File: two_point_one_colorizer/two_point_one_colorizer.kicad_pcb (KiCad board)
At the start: 2 copper layers, 100 x 100 mm, 83 parts, among them J1 rca, J2 rca, J3 Mini-DIN-4, J4 Barrel_Jack, J5 Conn_01x03, Q1 2N3904, SW1 SW_SPDT, SW2 SW_SPDT, U1 74HC14, U2 4053, U3 LM317, U4 LM1881, U5 74HC86, U6 4013, U7 LM393, U8 74LS221, U9 74LS221, Y1 Crystal

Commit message: revised all boards
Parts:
- added J6: Conn_01x03, Connector_PinHeader_2.54mm:PinHeader_1x03_P2.54mm_Vertical, F.Cu at (107.6, 92.2)
- added J7: Conn_02x08_Odd_Even, Connector_PinHeader_2.54mm:PinHeader_2x08_P2.54mm_Vertical, F.Cu at (182.9, 37.3)
- added R35: 1.5k, Resistor_THT:R_Axial_DIN0207_L6.3mm_D2.5mm_P7.62mm_Horizontal, F.Cu at (144.0, 47.9)
- added Y2: Crystal, Crystal:Crystal_HC49-4H_Vertical, F.Cu at (114.8, 92.5)
- J1, J2: footprint lib_fp:RCJ-024 -> lib_fp:tht_vertical_rca
- J3: value Mini-DIN-4 -> mini-din4; footprint lib_fp:MiniDin4-MD-40S -> lib_fp:mini-din-4-vertical_KMDVLX-4S-N-1
- R10: value 10k -> 1k
- R14: value 12k -> 1.5k
- R2: value 5k -> 5.1k
- R23, R29: value R -> 10k
- R26, R32: value 8.2k -> (lower than) 8.2k
- R7: value 1M -> 1m
- R9: value 1k -> 10k
- RV1, RV2, RV3, RV4, RV5, RV6: value 10k -> 10k_pot
- SW1, SW2: value SW_SPDT -> SPDT
- U2: value 4053 -> CD4053
- U6: value 4013 -> CD4013
- moved Y1 7.76 mm to (114.8, 86.4)
- moved J3 7.00 mm to (121.6, 43.8)
- moved C1 6.89 mm to (111.7, 81.9)
- moved C2 6.89 mm to (115.2, 81.9)
- moved C12 0.70 mm to (146.5, 62.2)
- moved R10 0.70 mm to (151.5, 54.7)
- moved R11 0.70 mm to (144.0, 58.2)
- moved R9 0.70 mm to (144.0, 51.2)
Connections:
- R10 pad 1: GND -> /sync_and_burst/black_and_sync
- U2 pad 3: GND -> /sync_and_burst/black_and_sync
- U6 pad 3: Net-(U4-Pad3) -> Net-(R10-Pad2)
- Y1 pad 1: Net-(C1-Pad1) -> Net-(J6-Pad3)
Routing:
- net Net-(R10-Pad2): track 15.1 -> 86.4 mm
- net Net-(U4-Pad3): track 68.4 -> 0.40 mm, vias 3 -> 0
- net /sync_and_burst/black_and_sync: track 0.00 -> 39.7 mm
- net Net-(C1-Pad1): track 21.3 -> 35.4 mm
- net +5V: track 560.3 -> 573.8 mm
- net Net-(J6-Pad3): track 0.00 -> 7.50 mm
- net Net-(J6-Pad1): track 0.00 -> 7.32 mm
- net Net-(C3-Pad2): track 24.4 -> 30.6 mm
- net GND: track 14.8 -> 20.4 mm
- net Net-(C2-Pad1): track 15.8 -> 18.7 mm
- net /sync_and_burst/burst_pulse: track 83.8 -> 84.5 mm
- net Net-(C15-Pad1): vias 1 -> 0
- net /colours/crystal: vias 1 -> 0
- net /colours/colour2: vias 2 -> 0
- net /colours/colour1: vias 3 -> 0
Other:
- board text added: "_^ XX"
- board text added: "two_point_one_colorizer v0_2 based on rob schafer design updated by cyberboy666"
- board text added: "underscores.shop"
- board text removed: "two_point_one_colorizer v0.1 by rob schafer pcb by cyberboy666"

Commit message: working on nexr version for colorizer and inverter
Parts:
- removed J5, J6: Conn_01x03, Connector_PinHeader_2.54mm:PinHeader_1x03_P2.54mm_Vertical
- removed REF** (x4): MountingHole_3.2mm_M3, MountingHole:MountingHole_3.2mm_M3
- added C21: 0.1n, Capacitor_THT:C_Disc_D4.7mm_W2.5mm_P5.00mm, F.Cu at (249.4, 78.2)
- added R36: 10k, Resistor_THT:R_Axial_DIN0207_L6.3mm_D2.5mm_P7.62mm_Horizontal, F.Cu at (211.4, 100.1)
- added RV7: 5k_trim, lib_fp:Pot_trim_3362_tayda, F.Cu at (213.6, 112.8)
- added RV8: 5k_trim, lib_fp:Pot_trim_3362_tayda, F.Cu at (221.5, 112.8)
- added RV9: 20k_pot, lib_fp:Potentiometer_Vertical_Large, F.Cu at (234.7, 86.2)
- added SW3: SPDT_slide, lib_fp:spdt_slide_switch_small_tayda, F.Cu at (279.9, 79.7)
- added SW4: SPDT_slide, lib_fp:spdt_slide_switch_small_tayda, F.Cu at (228.9, 99.1)
- added U11: 74HC4538, Package_DIP:DIP-16_W7.62mm_LongPads, F.Cu at (211.8, 78.3)
- R26, R32: value (lower than) 8.2k -> 1.5k
- R35: value 1.5k -> 1k (or 1.2k maybe)
- U1: value 74HC14 -> 4069
- U4: footprint Package_DIP:DIP-8_W7.62mm_LongPads -> lib_fp:DIP-SOIC-8
- moved U1 157.1 mm to (262.8, 78.3)
- moved U6 30.2 mm to (223.4, 78.3)
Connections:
- J3 pad 3: Net-(C3-Pad2) -> Net-(J3-Pad3)
- J3 pad 4: Net-(J3-Pad4) -> Net-(C3-Pad2)
- R26 pad 1: +5V -> Net-(R26-Pad1)
- R32 pad 1: +5V -> Net-(R32-Pad1)
- R9 pad 1: Net-(R10-Pad2) -> +5V
- R9 pad 2: +5V -> Net-(R10-Pad2)
- U4 pad 5: /sync_and_burst/burst_pulse -> Net-(U4-Pad5)
- U6 pad 6: +5V -> GND
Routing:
- net Net-(R10-Pad2): track 86.4 -> 62.2 mm
- net Net-(SW4-Pad3): track 22.4 -> 0.00 mm
- net Net-(J5-Pad1): track 0.00 -> 22.4 mm
- net +5V: track 573.8 -> 566.2 mm
- net Net-(C3-Pad2): track 30.6 -> 29.3 mm
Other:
- board text added: "two_point_one_colorizer v0_3 based on rob schafer design updated by cyberboy666"
- board text removed: "two_point_one_colorizer v0_2 based on rob schafer design updated by cyberboy666"

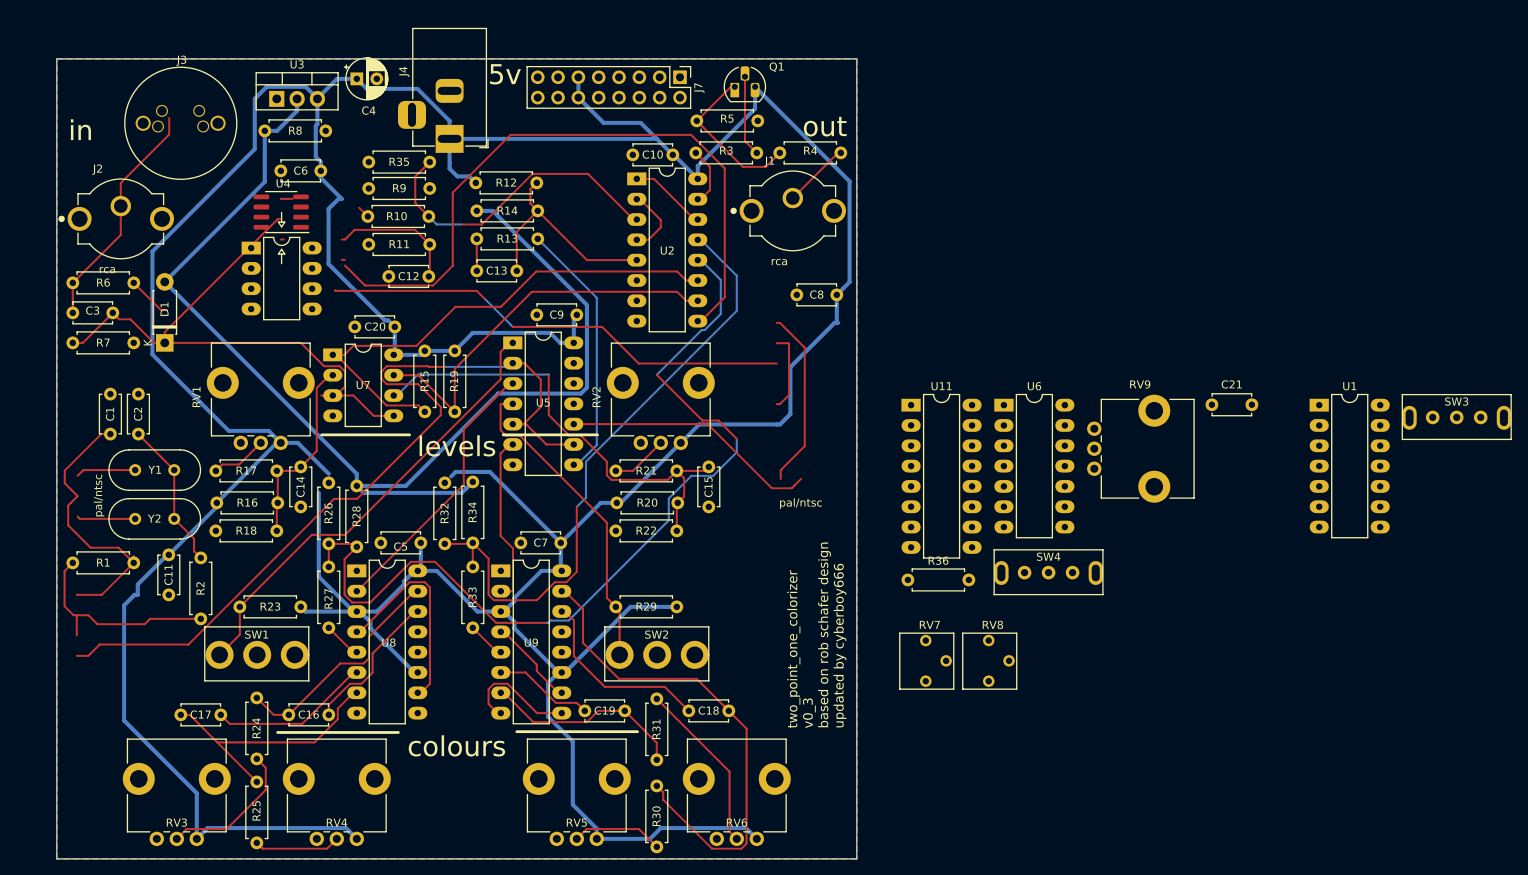
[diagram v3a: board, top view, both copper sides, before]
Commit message: lay out colorizer
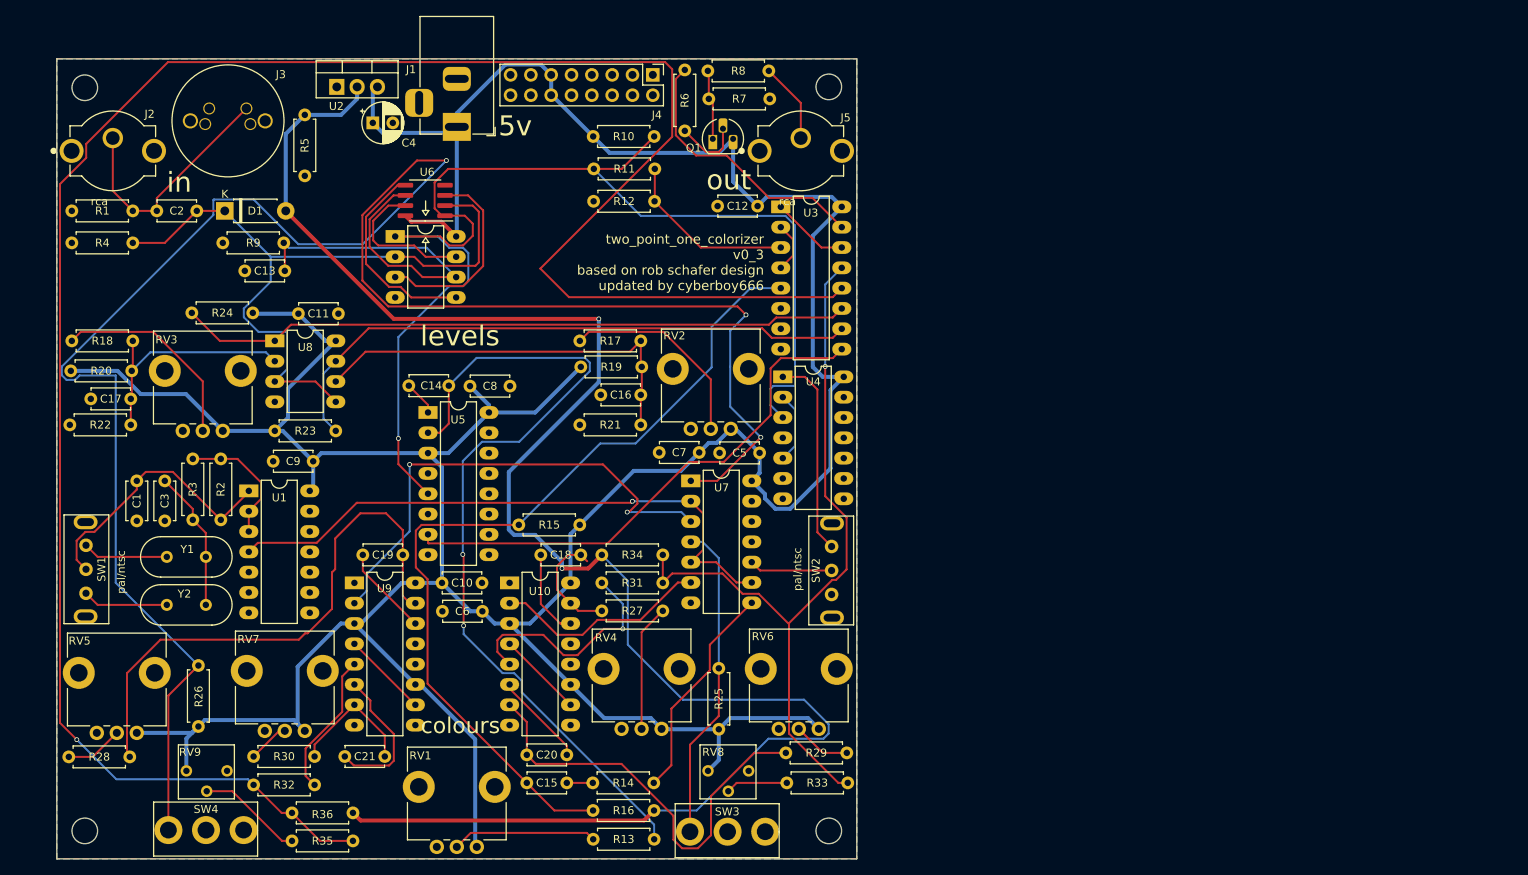
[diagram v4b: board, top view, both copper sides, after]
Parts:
- removed J7: Conn_02x08_Odd_Even, Connector_PinHeader_2.54mm:PinHeader_2x08_P2.54mm_Vertical
- removed U11: 74HC4538, Package_DIP:DIP-16_W7.62mm_LongPads
- added J5: rca, lib_fp:tht_vertical_rca, F.Cu at (198.0, 46.5)
- added REF**: MountingHole_3.2mm_M3, MountingHole:MountingHole_3.2mm_M3, F.Cu at (201.5, 38.5)
- added REF**: MountingHole_3.2mm_M3, MountingHole:MountingHole_3.2mm_M3, F.Cu at (201.5, 131.5)
- added REF**: MountingHole_3.2mm_M3, MountingHole:MountingHole_3.2mm_M3, F.Cu at (108.5, 131.5)
- added REF**: MountingHole_3.2mm_M3, MountingHole:MountingHole_3.2mm_M3, F.Cu at (108.5, 38.6)
- added U10: 74LS221, Package_DIP:DIP-16_W7.62mm_LongPads, F.Cu at (161.6, 100.5)
- C1, C10, C11, C12, C13, C15, C18, C19, C5, C6, C7, C8, C9: footprint Capacitor_THT:C_Disc_D4.7mm_W2.5mm_P5.00mm -> lib_fp:C_Disc_D4.7mm_W2.5mm_P5.00mm
- C14: value 0.1u -> 0.1n; footprint Capacitor_THT:C_Disc_D4.7mm_W2.5mm_P5.00mm -> lib_fp:C_Disc_D4.7mm_W2.5mm_P5.00mm
- C16, C17: value 10p -> 0.1u; footprint Capacitor_THT:C_Disc_D4.7mm_W2.5mm_P5.00mm -> lib_fp:C_Disc_D4.7mm_W2.5mm_P5.00mm
- C2: value 33p -> 0.1u; footprint Capacitor_THT:C_Disc_D4.7mm_W2.5mm_P5.00mm -> lib_fp:C_Disc_D4.7mm_W2.5mm_P5.00mm
- C20: value 0.1u -> 10p; footprint Capacitor_THT:C_Disc_D4.7mm_W2.5mm_P5.00mm -> lib_fp:C_Disc_D4.7mm_W2.5mm_P5.00mm
- C21: value 0.1n -> 10p; footprint Capacitor_THT:C_Disc_D4.7mm_W2.5mm_P5.00mm -> lib_fp:C_Disc_D4.7mm_W2.5mm_P5.00mm
- C3: value 0.1u -> 33p; footprint Capacitor_THT:C_Disc_D4.7mm_W2.5mm_P5.00mm -> lib_fp:C_Disc_D4.7mm_W2.5mm_P5.00mm
- J1: value rca -> Barrel_Jack; footprint lib_fp:tht_vertical_rca -> Connector_BarrelJack:BarrelJack_Horizontal
- J4: value Barrel_Jack -> Conn_02x08_Odd_Even; footprint Connector_BarrelJack:BarrelJack_Horizontal -> Connector_PinHeader_2.54mm:PinHeader_2x08_P2.54mm_Vertical
- R1: value 1m -> 75; footprint Resistor_THT:R_Axial_DIN0207_L6.3mm_D2.5mm_P7.62mm_Horizontal -> lib_fp:R_Axial_DIN0207_L6.3mm_D2.5mm_P7.62mm_Horizontal
- R10: value 1k -> 10k; footprint Resistor_THT:R_Axial_DIN0207_L6.3mm_D2.5mm_P7.62mm_Horizontal -> lib_fp:R_Axial_DIN0207_L6.3mm_D2.5mm_P7.62mm_Horizontal
- R11: value 680k -> 1k; footprint Resistor_THT:R_Axial_DIN0207_L6.3mm_D2.5mm_P7.62mm_Horizontal -> lib_fp:R_Axial_DIN0207_L6.3mm_D2.5mm_P7.62mm_Horizontal
- R12: value 12k -> 1k (or 1.2k maybe); footprint Resistor_THT:R_Axial_DIN0207_L6.3mm_D2.5mm_P7.62mm_Horizontal -> lib_fp:R_Axial_DIN0207_L6.3mm_D2.5mm_P7.62mm_Horizontal
- R13, R17, R19, R20, R22, R30, R34, R8: footprint Resistor_THT:R_Axial_DIN0207_L6.3mm_D2.5mm_P7.62mm_Horizontal -> lib_fp:R_Axial_DIN0207_L6.3mm_D2.5mm_P7.62mm_Horizontal
- R14, R26: value 1.5k -> 10k; footprint Resistor_THT:R_Axial_DIN0207_L6.3mm_D2.5mm_P7.62mm_Horizontal -> lib_fp:R_Axial_DIN0207_L6.3mm_D2.5mm_P7.62mm_Horizontal
- R15: value 82k -> 12k; footprint Resistor_THT:R_Axial_DIN0207_L6.3mm_D2.5mm_P7.62mm_Horizontal -> lib_fp:R_Axial_DIN0207_L6.3mm_D2.5mm_P7.62mm_Horizontal
- R16: value 82k -> 1.5k; footprint Resistor_THT:R_Axial_DIN0207_L6.3mm_D2.5mm_P7.62mm_Horizontal -> lib_fp:R_Axial_DIN0207_L6.3mm_D2.5mm_P7.62mm_Horizontal
- R18: value 10k -> 22k; footprint Resistor_THT:R_Axial_DIN0207_L6.3mm_D2.5mm_P7.62mm_Horizontal -> lib_fp:R_Axial_DIN0207_L6.3mm_D2.5mm_P7.62mm_Horizontal
- R2: value 5.1k -> 1m; footprint Resistor_THT:R_Axial_DIN0207_L6.3mm_D2.5mm_P7.62mm_Horizontal -> lib_fp:R_Axial_DIN0207_L6.3mm_D2.5mm_P7.62mm_Horizontal
- R21: value 22k -> 10k; footprint Resistor_THT:R_Axial_DIN0207_L6.3mm_D2.5mm_P7.62mm_Horizontal -> lib_fp:R_Axial_DIN0207_L6.3mm_D2.5mm_P7.62mm_Horizontal
- R23: value 10k -> 82k; footprint Resistor_THT:R_Axial_DIN0207_L6.3mm_D2.5mm_P7.62mm_Horizontal -> lib_fp:R_Axial_DIN0207_L6.3mm_D2.5mm_P7.62mm_Horizontal
- R24: value 2.7k -> 82k; footprint Resistor_THT:R_Axial_DIN0207_L6.3mm_D2.5mm_P7.62mm_Horizontal -> lib_fp:R_Axial_DIN0207_L6.3mm_D2.5mm_P7.62mm_Horizontal
- R25: value 2.7k -> 10k; footprint Resistor_THT:R_Axial_DIN0207_L6.3mm_D2.5mm_P7.62mm_Horizontal -> lib_fp:R_Axial_DIN0207_L6.3mm_D2.5mm_P7.62mm_Horizontal
- R27: value 1k -> 2.7k; footprint Resistor_THT:R_Axial_DIN0207_L6.3mm_D2.5mm_P7.62mm_Horizontal -> lib_fp:R_Axial_DIN0207_L6.3mm_D2.5mm_P7.62mm_Horizontal
- R28: value 3.3k -> 2.7k; footprint Resistor_THT:R_Axial_DIN0207_L6.3mm_D2.5mm_P7.62mm_Horizontal -> lib_fp:R_Axial_DIN0207_L6.3mm_D2.5mm_P7.62mm_Horizontal
- R29: value 10k -> 2.7k; footprint Resistor_THT:R_Axial_DIN0207_L6.3mm_D2.5mm_P7.62mm_Horizontal -> lib_fp:R_Axial_DIN0207_L6.3mm_D2.5mm_P7.62mm_Horizontal
- R3: value 100 -> 5.1k; footprint Resistor_THT:R_Axial_DIN0207_L6.3mm_D2.5mm_P7.62mm_Horizontal -> lib_fp:R_Axial_DIN0207_L6.3mm_D2.5mm_P7.62mm_Horizontal
- R31: value 2.7k -> 1k; footprint Resistor_THT:R_Axial_DIN0207_L6.3mm_D2.5mm_P7.62mm_Horizontal -> lib_fp:R_Axial_DIN0207_L6.3mm_D2.5mm_P7.62mm_Horizontal
- R32: value 1.5k -> 1k; footprint Resistor_THT:R_Axial_DIN0207_L6.3mm_D2.5mm_P7.62mm_Horizontal -> lib_fp:R_Axial_DIN0207_L6.3mm_D2.5mm_P7.62mm_Horizontal
- R33: value 1k -> 1.5k; footprint Resistor_THT:R_Axial_DIN0207_L6.3mm_D2.5mm_P7.62mm_Horizontal -> lib_fp:R_Axial_DIN0207_L6.3mm_D2.5mm_P7.62mm_Horizontal
- R35: value 1k (or 1.2k maybe) -> 1.5k; footprint Resistor_THT:R_Axial_DIN0207_L6.3mm_D2.5mm_P7.62mm_Horizontal -> lib_fp:R_Axial_DIN0207_L6.3mm_D2.5mm_P7.62mm_Horizontal
- R36: value 10k -> 3.3k; footprint Resistor_THT:R_Axial_DIN0207_L6.3mm_D2.5mm_P7.62mm_Horizontal -> lib_fp:R_Axial_DIN0207_L6.3mm_D2.5mm_P7.62mm_Horizontal
- R4: value 75 -> 1m; footprint Resistor_THT:R_Axial_DIN0207_L6.3mm_D2.5mm_P7.62mm_Horizontal -> lib_fp:R_Axial_DIN0207_L6.3mm_D2.5mm_P7.62mm_Horizontal
- R5: value 1k -> 75; footprint Resistor_THT:R_Axial_DIN0207_L6.3mm_D2.5mm_P7.62mm_Horizontal -> lib_fp:R_Axial_DIN0207_L6.3mm_D2.5mm_P7.62mm_Horizontal
- R6: value 75 -> 100; footprint Resistor_THT:R_Axial_DIN0207_L6.3mm_D2.5mm_P7.62mm_Horizontal -> lib_fp:R_Axial_DIN0207_L6.3mm_D2.5mm_P7.62mm_Horizontal
- R7: value 1m -> 1k; footprint Resistor_THT:R_Axial_DIN0207_L6.3mm_D2.5mm_P7.62mm_Horizontal -> lib_fp:R_Axial_DIN0207_L6.3mm_D2.5mm_P7.62mm_Horizontal
- R9: value 10k -> 680k; footprint Resistor_THT:R_Axial_DIN0207_L6.3mm_D2.5mm_P7.62mm_Horizontal -> lib_fp:R_Axial_DIN0207_L6.3mm_D2.5mm_P7.62mm_Horizontal
- RV1: value 10k_pot -> 20k_pot
- RV7: value 5k_trim -> 10k_pot; footprint lib_fp:Pot_trim_3362_tayda -> lib_fp:Potentiometer_Vertical_Large
- RV9: value 20k_pot -> 5k_trim; footprint lib_fp:Potentiometer_Vertical_Large -> lib_fp:Pot_trim_3362_tayda
- SW1, SW2: value SPDT -> SPDT_slide; footprint lib_fp:mini_toggle_switch_tayda -> lib_fp:spdt_slide_switch_small_tayda
- SW3, SW4: value SPDT_slide -> SPDT; footprint lib_fp:spdt_slide_switch_small_tayda -> lib_fp:mini_toggle_switch_tayda
- U2: value CD4053 -> LM317; footprint Package_DIP:DIP-16_W7.62mm_LongPads -> Package_TO_SOT_THT:TO-220-3_Vertical
- U3: value LM317 -> CD4053; footprint Package_TO_SOT_THT:TO-220-3_Vertical -> Package_DIP:DIP-16_W7.62mm_LongPads
- U4: value LM1881 -> CD4013; footprint lib_fp:DIP-SOIC-8 -> Package_DIP:DIP-14_W7.62mm_LongPads
- U5: value 74HC86 -> 74HC4538; footprint Package_DIP:DIP-14_W7.62mm_LongPads -> Package_DIP:DIP-16_W7.62mm_LongPads
- U6: value CD4013 -> LM1881; footprint Package_DIP:DIP-14_W7.62mm_LongPads -> lib_fp:DIP-SOIC-8
- U7: value LM393 -> 74HC86; footprint Package_DIP:DIP-8_W7.62mm_LongPads -> Package_DIP:DIP-14_W7.62mm_LongPads
- U8: value 74LS221 -> LM393; footprint Package_DIP:DIP-16_W7.62mm_LongPads -> Package_DIP:DIP-8_W7.62mm_LongPads
- moved U1 134.2 mm to (129.0, 89.0)
- moved RV9 119.6 mm to (121.2, 124.0), turned to 270 degrees
- moved C21 112.3 mm to (146.0, 122.2), turned to 180 degrees
- moved SW4 108.3 mm to (123.6, 124.4)
- moved SW3 101.6 mm to (188.8, 124.6)
- moved R4 89.2 mm to (114.5, 58.0)
- moved R35 85.4 mm to (134.4, 132.8)
- moved R7 85.1 mm to (186.5, 40.0)
- moved R36 82.3 mm to (134.4, 129.2)
- moved R3 80.2 mm to (122.0, 85.0), turned to 270 degrees
- moved R6 78.8 mm to (183.5, 44.0), turned to 90 degrees
- moved RV7 77.9 mm to (136.0, 119.0), turned to 90 degrees
- moved U6 77.3 mm to (151.0, 51.0)
- moved R13 76.4 mm to (172.1, 132.6)
- moved R14 73.0 mm to (172.0, 125.5)
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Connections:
- C12 pad 1: GND -> +5V
- C12 pad 2: Net-(C12-Pad2) -> GND
- C13 pad 1: /sync_and_burst/burst_signal -> GND
- C14 pad 2: GND -> Net-(C14-Pad2)
- C15 pad 1: Net-(C15-Pad1) -> /sync_and_burst/burst_signal
- C15 pad 2: GND -> Net-(C15-Pad2)
- C16 pad 2: Net-(C16-Pad2) -> GND
- C17 pad 2: Net-(C17-Pad2) -> GND
- C2 pad 1: Net-(C2-Pad1) -> /comparators/video
- C2 pad 2: GND -> Net-(C2-Pad2)
- C20 pad 1: +5V -> Net-(C20-Pad1)
- C20 pad 2: GND -> Net-(C20-Pad2)
- C3 pad 1: /comparators/video -> Net-(C3-Pad1)
- C3 pad 2: Net-(C3-Pad2) -> GND
- J1 pad 1: Net-(J1-Pad1) -> +5V
- J2 pad 1: Net-(C3-Pad2) -> Net-(C2-Pad2)
- J3 pad 4: Net-(C3-Pad2) -> Net-(C2-Pad2)
- J4 pad 1: +5V -> Net-(J4-Pad1)
- J4 pad 2: GND -> Net-(J4-Pad2)
- R1 pad 1: Net-(R1-Pad1) -> Net-(C2-Pad2)
- R1 pad 2: Net-(C1-Pad1) -> GND
- R10 pad 1: /sync_and_burst/black_and_sync -> +5V
- R11 pad 1: GND -> /sync_and_burst/black_and_sync
- R11 pad 2: Net-(C12-Pad2) -> Net-(R10-Pad2)
- R12 pad 1: /sync_and_burst/burst_signal -> GND
- R12 pad 2: +5V -> /sync_and_burst/black_and_sync
- R13 pad 1: Net-(C13-Pad2) -> Net-(R13-Pad1)
- R13 pad 2: Net-(R13-Pad2) -> Net-(C14-Pad1)
- R14 pad 1: 1.25v -> Net-(C15-Pad2)
- R14 pad 2: /sync_and_burst/burst_signal -> Net-(R14-Pad2)
- R15 pad 1: +5V -> /sync_and_burst/burst_signal
- R15 pad 2: /comparators/comparator1 -> +5V
- R16 pad 1: +5V -> 1.25v
- R16 pad 2: Net-(C14-Pad1) -> /sync_and_burst/burst_signal
- R17 pad 1: Net-(C14-Pad1) -> Net-(C16-Pad1)
- R18 pad 1: Net-(C14-Pad1) -> Net-(C17-Pad1)
- R18 pad 2: GND -> Net-(R18-Pad2)
- R19 pad 2: /comparators/comparator2 -> Net-(C16-Pad1)
- R2 pad 1: Net-(R1-Pad1) -> Net-(R2-Pad1)
- R2 pad 2: Net-(C2-Pad1) -> Net-(C1-Pad1)
- R20 pad 2: Net-(C15-Pad1) -> Net-(C17-Pad1)
- R21 pad 1: Net-(C15-Pad1) -> Net-(C16-Pad1)
- R21 pad 2: Net-(R21-Pad2) -> GND
- R22 pad 1: Net-(C15-Pad1) -> Net-(C17-Pad1)
- R23 pad 2: Net-(R23-Pad2) -> /comparators/comparator2
- R24 pad 1: Net-(R24-Pad1) -> +5V
- R24 pad 2: Net-(C16-Pad1) -> /comparators/comparator1
- R25 pad 1: Net-(R25-Pad1) -> +5V
- R25 pad 2: Net-(C17-Pad1) -> Net-(R25-Pad2)
- R26 pad 1: Net-(R26-Pad1) -> +5V
- R26 pad 2: /colours/colour1 -> Net-(R26-Pad2)
- R27 pad 1: /colours/colour1 -> Net-(R27-Pad1)
- R27 pad 2: Net-(R27-Pad2) -> Net-(C18-Pad1)
- R28 pad 1: /colours/colour1 -> Net-(R28-Pad1)
- R28 pad 2: 1.25v -> Net-(C19-Pad1)
- R29 pad 1: +5V -> Net-(R29-Pad1)
- R29 pad 2: Net-(R29-Pad2) -> Net-(C20-Pad1)
- R3 pad 1: Net-(Q1-Pad2) -> Net-(R2-Pad1)
- R3 pad 2: Net-(R3-Pad2) -> Net-(C3-Pad1)
- R30 pad 2: Net-(C18-Pad1) -> Net-(C21-Pad1)
- R31 pad 1: Net-(R31-Pad1) -> /colours/colour2
- R31 pad 2: Net-(C19-Pad1) -> Net-(R31-Pad2)
- R32 pad 1: Net-(R32-Pad1) -> /colours/colour1
- R32 pad 2: /colours/colour2 -> Net-(R32-Pad2)
- R33 pad 1: /colours/colour2 -> Net-(R33-Pad1)
- R33 pad 2: Net-(R33-Pad2) -> /colours/colour2
- R35 pad 1: GND -> Net-(R35-Pad1)
- R35 pad 2: /sync_and_burst/black_and_sync -> /colours/colour1
- R36 pad 1: Net-(R36-Pad1) -> /colours/colour1
- R36 pad 2: Net-(C21-Pad1) -> 1.25v
- R4 pad 1: Net-(J1-Pad1) -> /comparators/video
- R4 pad 2: Net-(Q1-Pad1) -> GND
- R5 pad 1: Net-(Q1-Pad1) -> 1.25v
- R6 pad 1: Net-(C3-Pad2) -> Net-(Q1-Pad2)
- R6 pad 2: GND -> Net-(R6-Pad2)
- R7 pad 1: /comparators/video -> Net-(Q1-Pad1)
- R8 pad 1: 1.25v -> Net-(J5-Pad1)
- R8 pad 2: GND -> Net-(Q1-Pad1)
- R9 pad 1: +5V -> GND
- R9 pad 2: Net-(R10-Pad2) -> Net-(C13-Pad2)
- RV1 pad 2: Net-(R17-Pad2) -> Net-(R13-Pad1)
- RV1 pad 3: GND -> Net-(RV1-Pad3)
- RV2 pad 2: Net-(R21-Pad2) -> Net-(R17-Pad2)
- RV3 pad 2: Net-(R24-Pad1) -> Net-(R18-Pad2)
- RV3 pad 3: Net-(RV3-Pad3) -> GND
- RV4 pad 2: Net-(R25-Pad1) -> Net-(R27-Pad1)
- RV5 pad 2: Net-(R30-Pad1) -> Net-(R28-Pad1)
- RV6 pad 2: Net-(R31-Pad1) -> Net-(R29-Pad1)
- RV7 pad 2: Net-(R32-Pad1) -> Net-(R30-Pad1)
- RV8 pad 2: Net-(R26-Pad1) -> Net-(R33-Pad1)
- RV9 pad 2: Net-(R36-Pad1) -> Net-(R35-Pad1)
- SW1 pad 1: Net-(R23-Pad2) -> Net-(SW1-Pad1)
- SW1 pad 2: GND -> Net-(C1-Pad1)
- SW2 pad 1: Net-(R29-Pad2) -> GND
- SW2 pad 2: GND -> Net-(SW2-Pad2)
- SW3 pad 1: Net-(SW3-Pad1) -> Net-(R25-Pad2)
- SW3 pad 2: Net-(C1-Pad1) -> GND
- SW4 pad 1: GND -> Net-(R26-Pad2)
- SW4 pad 2: Net-(SW4-Pad2) -> GND
- U1 pad 2: Net-(R1-Pad1) -> Net-(R2-Pad1)
- U1 pad 3: Net-(R1-Pad1) -> Net-(R2-Pad1)
- U2 pad 1: colours -> GND
- U2 pad 2: black_sync_and_burst -> 1.25v
- U2 pad 3: /sync_and_burst/black_and_sync -> +5V
- U3 pad 1: GND -> colours
- U3 pad 2: 1.25v -> black_sync_and_burst
- U3 pad 3: +5V -> /sync_and_burst/black_and_sync
- U4 pad 1: Net-(R10-Pad2) -> Net-(SW2-Pad3)
- U4 pad 2: /comparators/video -> Net-(U4-Pad2)
- U4 pad 3: Net-(U4-Pad3) -> Net-(R10-Pad2)
- U4 pad 5: Net-(U4-Pad5) -> Net-(U4-Pad2)
- U4 pad 6: Net-(C12-Pad2) -> GND
- U4 pad 7: Net-(U4-Pad7) -> GND
- U4 pad 8: +5V -> Net-(U4-Pad8)
- U5 pad 1: Net-(R23-Pad2) -> Net-(C14-Pad2)
- U5 pad 10: Net-(SW4-Pad2) -> Net-(U5-Pad10)
- U5 pad 14: +5V -> Net-(U5-Pad14)
- U5 pad 2: /colours/crystal -> Net-(C14-Pad1)
- U5 pad 3: Net-(U5-Pad3) -> +5V
- U5 pad 4: Net-(R29-Pad2) -> GND
- U5 pad 5: /colours/crystal -> Net-(R10-Pad2)
- U5 pad 7: GND -> /sync_and_burst/burst_pulse
- U5 pad 8: Net-(R13-Pad2) -> GND
- U5 pad 9: /colours/crystal -> Net-(U5-Pad9)
- U6 pad 1: Net-(SW4-Pad3) -> Net-(R10-Pad2)
- U6 pad 2: Net-(U6-Pad2) -> /comparators/video
- U6 pad 3: Net-(R10-Pad2) -> Net-(U6-Pad3)
- U6 pad 5: Net-(U6-Pad2) -> Net-(U6-Pad5)
- U6 pad 6: GND -> Net-(C13-Pad2)
- U6 pad 7: GND -> Net-(U6-Pad7)
- U6 pad 8: Net-(U6-Pad8) -> +5V
- U7 pad 1: /comparators/comparator1 -> Net-(R26-Pad2)
- U7 pad 2: Net-(C14-Pad1) -> /colours/crystal
- U7 pad 3: /comparators/video -> Net-(U7-Pad3)
- U7 pad 4: GND -> Net-(R25-Pad2)
- U7 pad 5: /comparators/video -> /colours/crystal
- U7 pad 6: Net-(C15-Pad1) -> Net-(U10-Pad2)
- U7 pad 7: /comparators/comparator2 -> GND
- U7 pad 8: +5V -> Net-(R14-Pad2)
- U8 pad 1: GND -> /comparators/comparator1
- U8 pad 2: Net-(U5-Pad3) -> Net-(C17-Pad1)
- U8 pad 3: +5V -> /comparators/video
- U8 pad 4: Net-(U8-Pad10) -> GND
- U8 pad 5: Net-(R27-Pad2) -> /comparators/video
- U8 pad 6: Net-(C17-Pad2) -> Net-(C16-Pad1)
- U8 pad 7: Net-(C17-Pad1) -> /comparators/comparator2
- U8 pad 8: GND -> +5V
- U9 pad 14: Net-(C18-Pad2) -> Net-(C19-Pad2)
- U9 pad 15: Net-(C18-Pad1) -> Net-(C19-Pad1)
- U9 pad 2: Net-(U5-Pad6) -> Net-(U7-Pad3)
- U9 pad 5: Net-(R33-Pad2) -> Net-(R32-Pad2)
- U9 pad 6: Net-(C19-Pad2) -> Net-(C21-Pad2)
- U9 pad 7: Net-(C19-Pad1) -> Net-(C21-Pad1)
- Y1 pad 1: Net-(SW3-Pad1) -> Net-(SW1-Pad1)
- Y1 pad 2: Net-(C2-Pad1) -> Net-(C3-Pad1)
- Y2 pad 1: Net-(SW3-Pad3) -> Net-(SW1-Pad3)
- Y2 pad 2: Net-(C2-Pad1) -> Net-(C3-Pad1)
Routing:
- net Net-(R26-Pad2): track 0.00 -> 235.4 mm, vias 0 -> 3
- net /colours/colour1: track 112.6 -> 265.7 mm, vias 0 -> 1
- net Net-(R10-Pad2): track 62.2 -> 152.6 mm, vias 0 -> 1
- net Net-(C14-Pad1): track 24.2 -> 106.8 mm, vias 0 -> 2
- net +5V: track 566.2 -> 485.7 mm
- net /sync_and_burst/burst_signal: track 27.7 -> 108.1 mm
- net 1.25v: track 144.3 -> 219.7 mm, vias 0 -> 2
- net Net-(U7-Pad3): track 0.00 -> 61.2 mm, vias 0 -> 2
- net Net-(C15-Pad1): track 58.8 -> 0.00 mm
- net Net-(R23-Pad2): track 56.8 -> 0.00 mm
- net Net-(C20-Pad1): track 0.00 -> 53.9 mm
- net Net-(C18-Pad1): track 63.5 -> 14.3 mm
- net Net-(C13-Pad2): track 4.00 -> 48.4 mm
- net Net-(C19-Pad1): track 25.4 -> 69.3 mm
- net Net-(R29-Pad2): track 40.0 -> 0.00 mm
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
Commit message: newest circuit revisions
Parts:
- moved SW2 0.39 mm to (202.1, 98.8), turned to 270 degrees
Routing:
- net GND: track 0.00 -> 40.5 mm, vias 0 -> 2
- net Net-(SW2-Pad3): track 25.3 -> 32.5 mm
- net /colours/colour2: track 95.7 -> 97.5 mm
- net Net-(R10-Pad2): track 152.6 -> 153.8 mm
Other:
- board text added: "IN"
- board text added: "OUT"
- board text removed: "in"
- board text removed: "out"
